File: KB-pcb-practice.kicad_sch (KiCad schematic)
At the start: 49 parts, among them J1 SWD, SW1 Boot, SW2 Reset, U1 NCP1117-3.3_SOT223, U1 W25Q128JVS, Y1 ABLS-12.000MHZ-B4-T

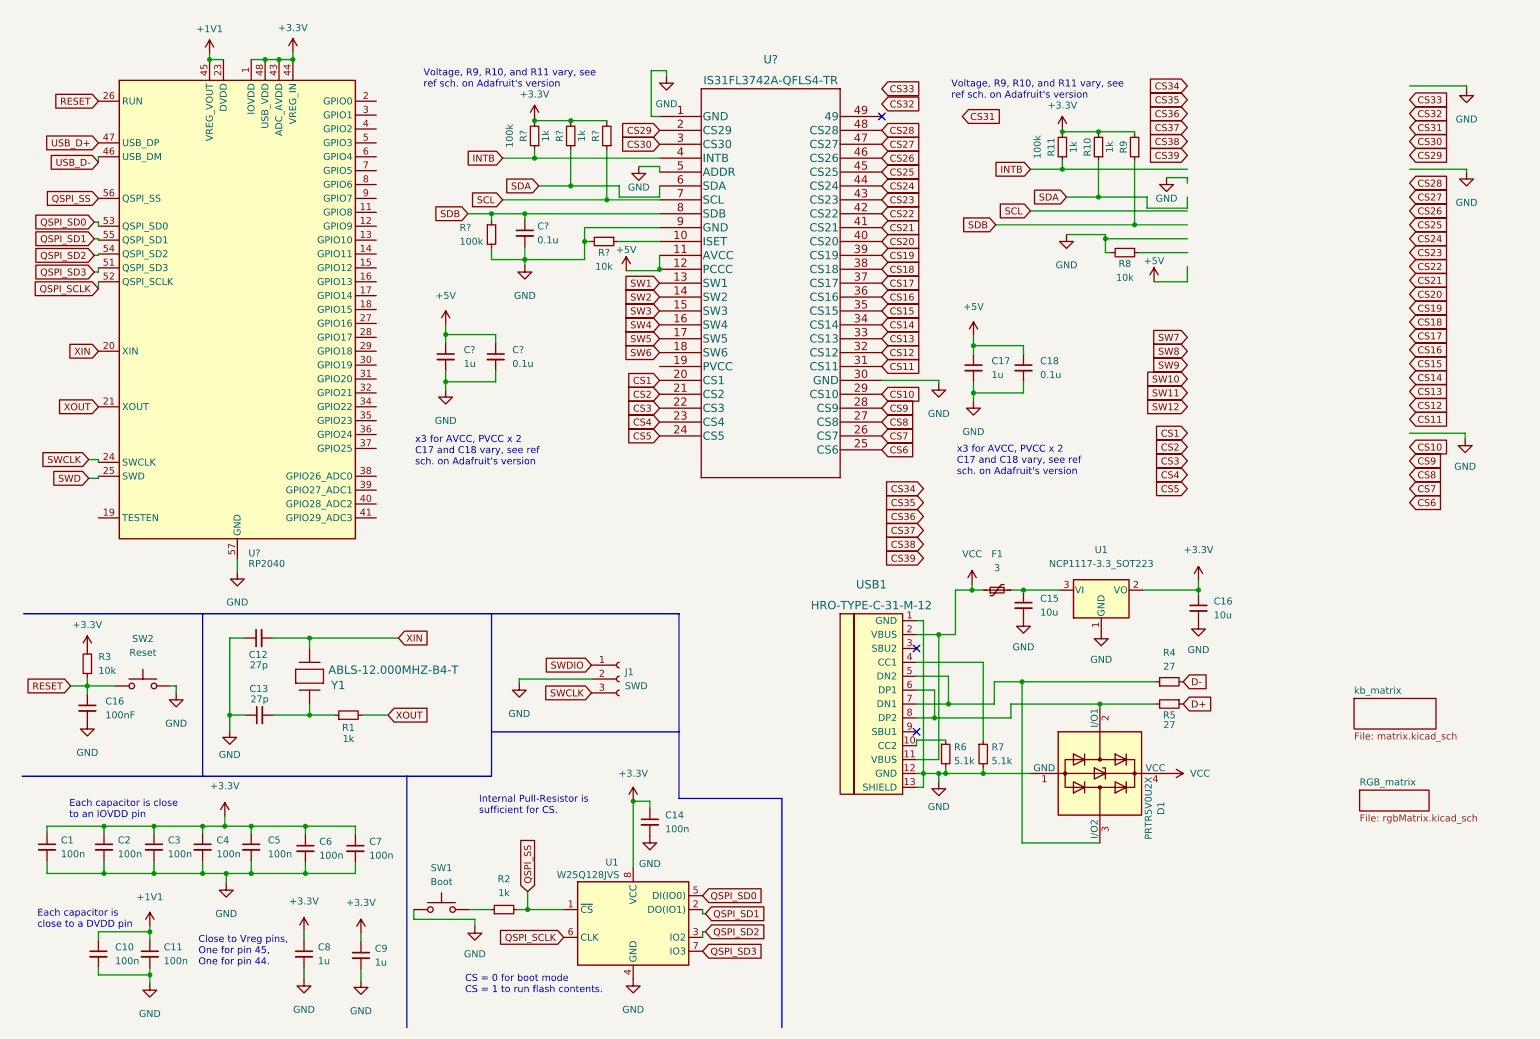
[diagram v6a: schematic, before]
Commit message: Finished Electric Schematic Of Keyboard
All components are now wired. Positions for spacers, button stabilizers, and threated holes not accounted.
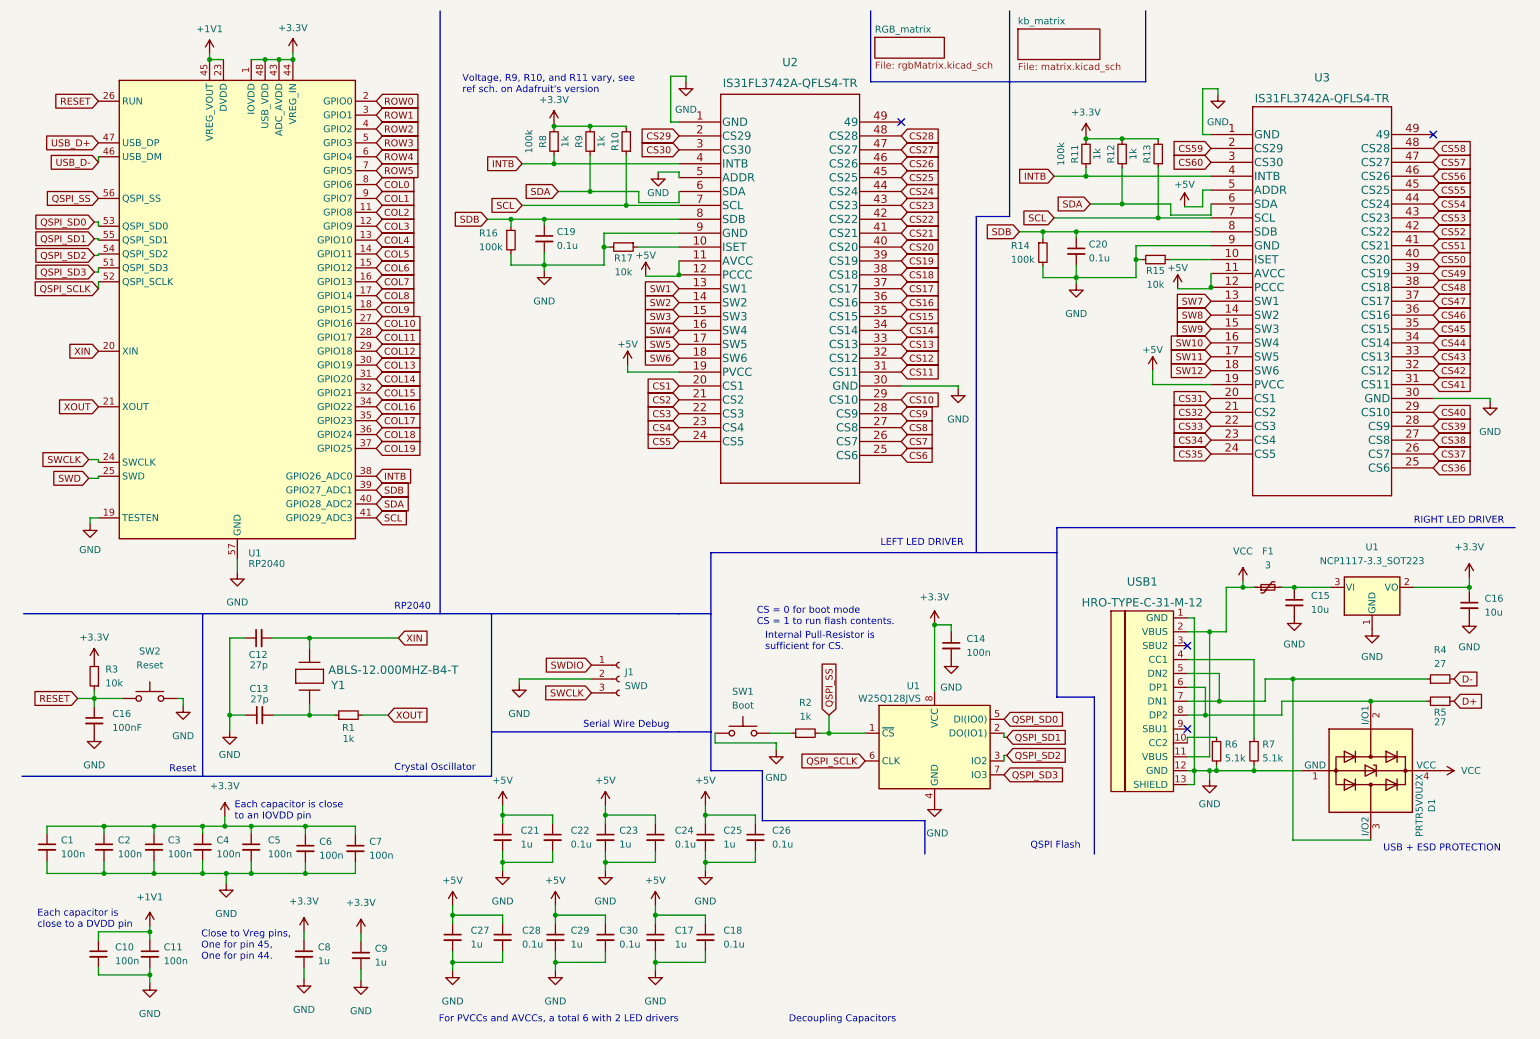
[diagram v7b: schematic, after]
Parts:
- removed R10, R9: 1k, symbol Device:R_Small
- removed R8: 10k, symbol Device:R_Small
- added C20, C22, C24, C26, C28: 0.1u, symbol Device:C_Small
- added C21, C23, C25, C27: 1u, symbol Device:C_Small
- added R12, R13: 1k, symbol Device:R_Small
- added R14: 100k, symbol Device:R_Small
- added R15: 10k, symbol Device:R_Small
- added U3: IS31FL3742A-QFLS4-TR, QFN48_IS31FL3742A-QFLS4-TR_ISI, symbol ul_IS31FL3742A-QFLS4-TR:IS31FL3742A-QFLS4-TR
- gave numbers to parts that had none: 10
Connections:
- net +3.3V: now also R12.2, R13.2
- net +5V: now also U2.19 (PVCC), C21.1, C22.1, C23.1, C24.1, C25.1, C26.1, C27.1, C28.1, U3.11 (AVCC), U3.12 (PCCC), U3.19 (PVCC), U3.5 (ADDR)
- net CS31: now also U3.20 (CS1)
- net CS32: now also U3.21 (CS2)
- net CS33: now also U3.22 (CS3)
- net CS34: now also U3.23 (CS4)
- net CS35: now also U3.24 (CS5)
- net CS36: now also U3.25 (CS6)
- net CS37: now also U3.26 (CS7)
- net CS38: now also U3.27 (CS8)
- net CS39: now also U3.28 (CS9)
- net GND: now also U1.19 (TESTEN), C20.2, C21.2, C22.2, C23.2, C24.2, C25.2, C26.2, C27.2, C28.2, R14.2, R15.2, U3.1 (GND), U3.30 (GND), U3.9 (GND)
- net INTB: now also U1.38 (GPIO26_ADC0), U3.4 (INTB)
- net SCL: now also U1.41 (GPIO29_ADC3), R13.1, U3.7 (SCL)
- net SDA: now also U1.40 (GPIO28_ADC2), R12.1, U3.6 (SDA)
- net SDB: now also U1.39 (GPIO27_ADC1), C20.1, R14.1, U3.8 (SDB)
- net SW10: now also U3.16 (SW4)
- net SW11: now also U3.17 (SW5)
- net SW12: now also U3.18 (SW6)
- net SW7: now also U3.13 (SW1)
- net SW8: now also U3.14 (SW2)
- net SW9: now also U3.15 (SW3)
- net COL2: now reaches U1.11 (GPIO8)
- net COL3: now reaches U1.12 (GPIO9)
- net COL4: now reaches U1.13 (GPIO10)
- net COL5: now reaches U1.14 (GPIO11)
- net COL6: now reaches U1.15 (GPIO12)
- net COL7: now reaches U1.16 (GPIO13)
- net COL8: now reaches U1.17 (GPIO14)
- net COL9: now reaches U1.18 (GPIO15)
- net ROW0: now reaches U1.2 (GPIO0)
- net COL10: now reaches U1.27 (GPIO16)
- net COL11: now reaches U1.28 (GPIO17)
- net COL12: now reaches U1.29 (GPIO18)
- net ROW1: now reaches U1.3 (GPIO1)
- net COL13: now reaches U1.30 (GPIO19)
- net COL14: now reaches U1.31 (GPIO20)
- net COL15: now reaches U1.32 (GPIO21)
- net COL16: now reaches U1.34 (GPIO22)
- net COL17: now reaches U1.35 (GPIO23)
- net COL18: now reaches U1.36 (GPIO24)
- net COL19: now reaches U1.37 (GPIO25)
- net ROW2: now reaches U1.4 (GPIO2)
- net ROW3: now reaches U1.5 (GPIO3)
- net ROW4: now reaches U1.6 (GPIO4)
- net ROW5: now reaches U1.7 (GPIO5)
- net COL0: now reaches U1.8 (GPIO6)
- net COL1: now reaches U1.9 (GPIO7)
- new net: R15.1, U3.10 (ISET)
- new net CS40: U3.29 (CS10)
- new net CS41: U3.31 (CS11)
- new net CS42: U3.32 (CS12)
- new net CS43: U3.33 (CS13)
- new net CS44: U3.34 (CS14)
- new net CS45: U3.35 (CS15)
- new net CS46: U3.36 (CS16)
- new net CS47: U3.37 (CS17)
- new net CS48: U3.38 (CS18)
- new net CS49: U3.39 (CS19)
- new net CS50: U3.40 (CS20)
- new net CS51: U3.41 (CS21)
- new net CS52: U3.42 (CS22)
- new net CS53: U3.43 (CS23)
- new net CS54: U3.44 (CS24)
- new net CS55: U3.45 (CS25)
- new net CS56: U3.46 (CS26)
- new net CS57: U3.47 (CS27)
- new net CS58: U3.48 (CS28)
- new net CS59: U3.2 (CS29)
- new net CS60: U3.3 (CS30)
- no-connect marks 3 -> 4
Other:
- note added: "Crystal Oscillator"
- note added: "Decoupling Capacitors"
- note added: "For PVCCs and AVCCs, a total 6 with 2 LED drivers"
- note added: "LEFT LED DRIVER"
- note added: "QSPI Flash"
- note added: "RIGHT LED DRIVER"
- note added: "RP2040"
- note added: "Reset"
- note added: "Serial Wire Debug"
- note added: "USB + ESD PROTECTION"
- note removed: "x3 for AVCC, PVCC x 2 C17 and C18 vary, see ref sch. on Adafruit's version"
- moved on the sheet: C14, C15, C16, C19, C29, C30, D1, F1, R10, R16, R17, R2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

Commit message: Started work on PCB layout
Slightly Adjusted electric schematic as well.
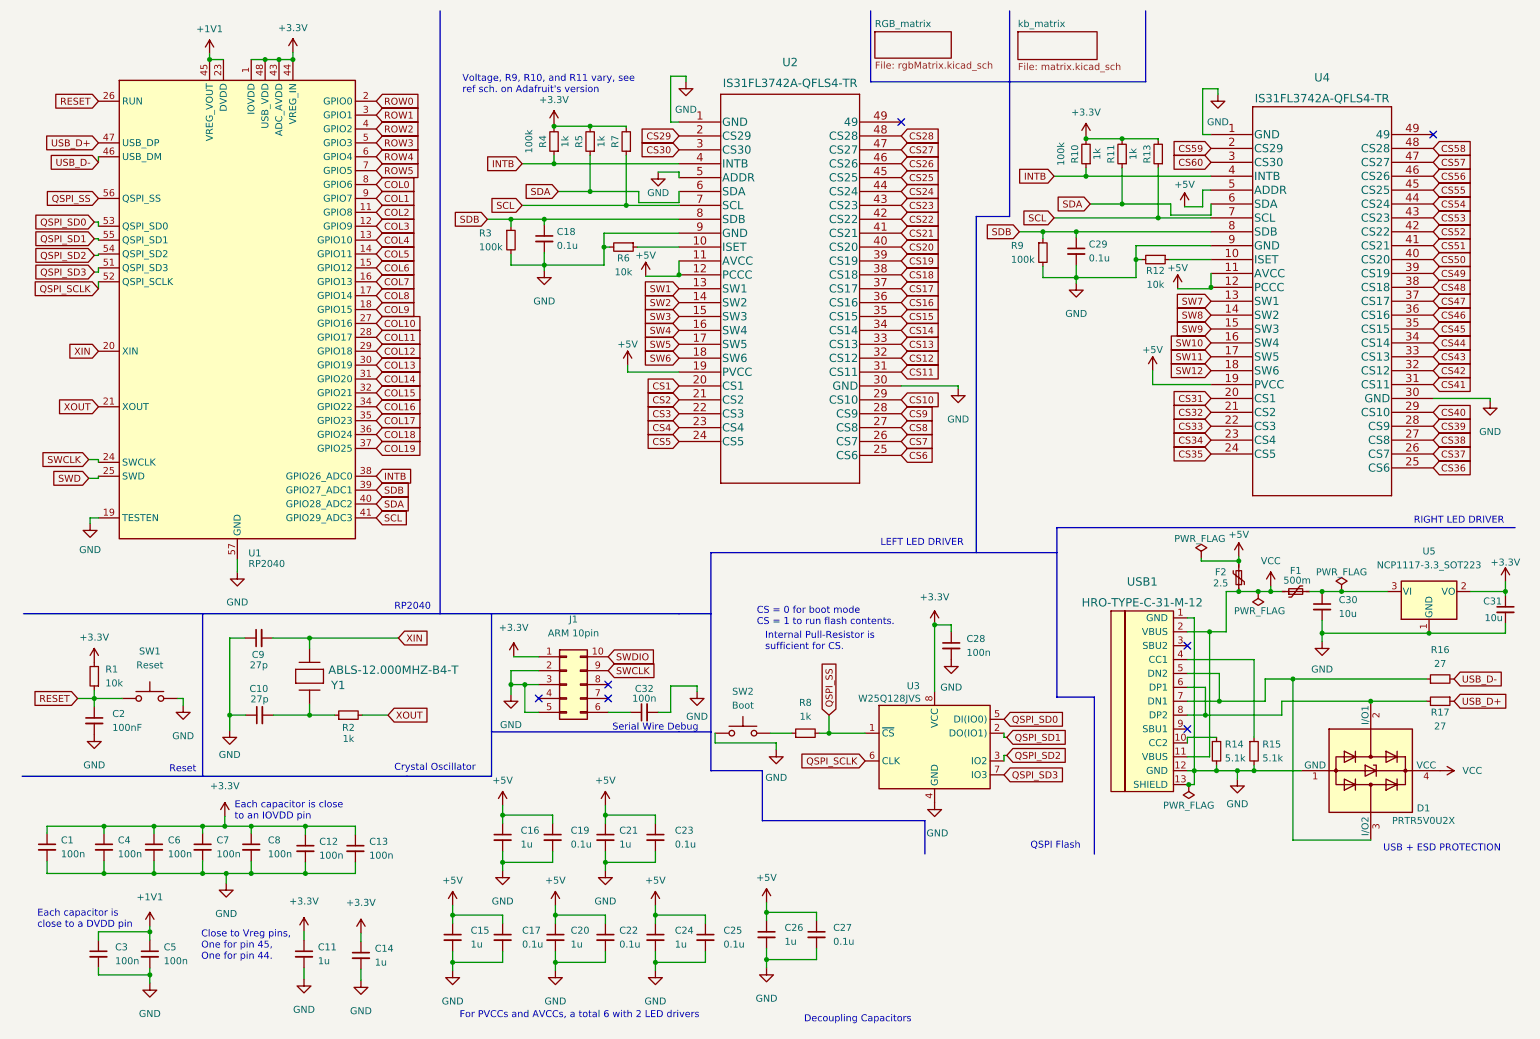
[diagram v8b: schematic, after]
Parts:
- removed J1: SWD, symbol Connector:Conn_01x03_Female
- added C32: 100n, Capacitor_SMD:C_0805_2012Metric_Pad1.18x1.45mm_HandSolder, symbol Device:C_Small
- added F2: 2.5, Fuse:Fuse_1206_3216Metric_Pad1.42x1.75mm_HandSolder, symbol Device:Polyfuse_Small
- added J1: ARM 10pin, Connector_PinHeader_1.27mm:PinHeader_2x05_P1.27mm_Horizontal, symbol Connector_Generic:Conn_02x05_Counter_Clockwise
- C1: footprint (none) -> Capacitor_SMD:C_0805_2012Metric_Pad1.18x1.45mm_HandSolder
- C10: renamed from C13; footprint (none) -> Capacitor_SMD:C_0805_2012Metric_Pad1.18x1.45mm_HandSolder
- C11: renamed from C8; footprint (none) -> Capacitor_SMD:C_0805_2012Metric_Pad1.18x1.45mm_HandSolder
- C12: renamed from C6; footprint (none) -> Capacitor_SMD:C_0805_2012Metric_Pad1.18x1.45mm_HandSolder
- C13: renamed from C7; footprint (none) -> Capacitor_SMD:C_0805_2012Metric_Pad1.18x1.45mm_HandSolder
- C14: renamed from C9; footprint (none) -> Capacitor_SMD:C_0805_2012Metric_Pad1.18x1.45mm_HandSolder
- C15: renamed from C27; footprint (none) -> Capacitor_SMD:C_0805_2012Metric_Pad1.18x1.45mm_HandSolder
- C16: renamed from C21; footprint (none) -> Capacitor_SMD:C_0805_2012Metric_Pad1.18x1.45mm_HandSolder
- C17: renamed from C28; footprint (none) -> Capacitor_SMD:C_0805_2012Metric_Pad1.18x1.45mm_HandSolder
- C18: renamed from C19; footprint (none) -> Capacitor_SMD:C_0805_2012Metric_Pad1.18x1.45mm_HandSolder
- C19: renamed from C22; footprint (none) -> Capacitor_SMD:C_0805_2012Metric_Pad1.18x1.45mm_HandSolder
- C2, C31: renamed from C16; footprint (none) -> Capacitor_SMD:C_0805_2012Metric_Pad1.18x1.45mm_HandSolder
- C20: renamed from C29; footprint (none) -> Capacitor_SMD:C_0805_2012Metric_Pad1.18x1.45mm_HandSolder
- C21: renamed from C23; footprint (none) -> Capacitor_SMD:C_0805_2012Metric_Pad1.18x1.45mm_HandSolder
- C22: renamed from C30; footprint (none) -> Capacitor_SMD:C_0805_2012Metric_Pad1.18x1.45mm_HandSolder
- C23: renamed from C24; footprint (none) -> Capacitor_SMD:C_0805_2012Metric_Pad1.18x1.45mm_HandSolder
- C24: renamed from C17; footprint (none) -> Capacitor_SMD:C_0805_2012Metric_Pad1.18x1.45mm_HandSolder
- C25: renamed from C18; footprint (none) -> Capacitor_SMD:C_0805_2012Metric_Pad1.18x1.45mm_HandSolder
- C26: renamed from C25; footprint (none) -> Capacitor_SMD:C_0805_2012Metric_Pad1.18x1.45mm_HandSolder
- C27: renamed from C26; footprint (none) -> Capacitor_SMD:C_0805_2012Metric_Pad1.18x1.45mm_HandSolder
- C28: renamed from C14; footprint (none) -> Capacitor_SMD:C_0805_2012Metric_Pad1.18x1.45mm_HandSolder
- C29: renamed from C20; footprint (none) -> Capacitor_SMD:C_0805_2012Metric_Pad1.18x1.45mm_HandSolder
- C3: renamed from C10; footprint (none) -> Capacitor_SMD:C_0805_2012Metric_Pad1.18x1.45mm_HandSolder
- C30: renamed from C15; footprint (none) -> Capacitor_SMD:C_0805_2012Metric_Pad1.18x1.45mm_HandSolder
- C4: renamed from C2; footprint (none) -> Capacitor_SMD:C_0805_2012Metric_Pad1.18x1.45mm_HandSolder
- C5: renamed from C11; footprint (none) -> Capacitor_SMD:C_0805_2012Metric_Pad1.18x1.45mm_HandSolder
- C6: renamed from C3; footprint (none) -> Capacitor_SMD:C_0805_2012Metric_Pad1.18x1.45mm_HandSolder
- C7: renamed from C4; footprint (none) -> Capacitor_SMD:C_0805_2012Metric_Pad1.18x1.45mm_HandSolder
- C8: renamed from C5; footprint (none) -> Capacitor_SMD:C_0805_2012Metric_Pad1.18x1.45mm_HandSolder
- C9: renamed from C12; footprint (none) -> Capacitor_SMD:C_0805_2012Metric_Pad1.18x1.45mm_HandSolder
- F1: value 3 -> 500m; footprint (none) -> Fuse:Fuse_1206_3216Metric_Pad1.42x1.75mm_HandSolder
- R1: renamed from R3; footprint (none) -> Resistor_SMD:R_0805_2012Metric_Pad1.20x1.40mm_HandSolder
- R10: renamed from R11; footprint (none) -> Resistor_SMD:R_0805_2012Metric_Pad1.20x1.40mm_HandSolder
- R11: renamed from R12; footprint (none) -> Resistor_SMD:R_0805_2012Metric_Pad1.20x1.40mm_HandSolder
- R12: renamed from R15; footprint (none) -> Resistor_SMD:R_0805_2012Metric_Pad1.20x1.40mm_HandSolder
- R13: footprint (none) -> Resistor_SMD:R_0805_2012Metric_Pad1.20x1.40mm_HandSolder
- R14: renamed from R6; footprint (none) -> Resistor_SMD:R_0805_2012Metric_Pad1.20x1.40mm_HandSolder
- R15: renamed from R7; footprint (none) -> Resistor_SMD:R_0805_2012Metric_Pad1.20x1.40mm_HandSolder
- R16: renamed from R4; footprint (none) -> Resistor_SMD:R_0805_2012Metric_Pad1.20x1.40mm_HandSolder
- R17: renamed from R5; footprint (none) -> Resistor_SMD:R_0805_2012Metric_Pad1.20x1.40mm_HandSolder
- R2: renamed from R1; footprint (none) -> Resistor_SMD:R_0805_2012Metric_Pad1.20x1.40mm_HandSolder
- R3: renamed from R16; footprint (none) -> Resistor_SMD:R_0805_2012Metric_Pad1.20x1.40mm_HandSolder
- R4: renamed from R8; footprint (none) -> Resistor_SMD:R_0805_2012Metric_Pad1.20x1.40mm_HandSolder
- R5: renamed from R9; footprint (none) -> Resistor_SMD:R_0805_2012Metric_Pad1.20x1.40mm_HandSolder
- R6: renamed from R17; footprint (none) -> Resistor_SMD:R_0805_2012Metric_Pad1.20x1.40mm_HandSolder
- R7: renamed from R10; footprint (none) -> Resistor_SMD:R_0805_2012Metric_Pad1.20x1.40mm_HandSolder
- R8: renamed from R2; footprint (none) -> Resistor_SMD:R_0805_2012Metric_Pad1.20x1.40mm_HandSolder
- R9: renamed from R14; footprint (none) -> Resistor_SMD:R_0805_2012Metric_Pad1.20x1.40mm_HandSolder
- SW1: renamed from SW2; footprint (none) -> Button_Switch_SMD:SW_SPST_SKQG_WithStem
- SW2: renamed from SW1; footprint (none) -> Button_Switch_SMD:SW_SPST_SKQG_WithStem
- U2: footprint QFN48_IS31FL3742A-QFLS4-TR_ISI -> ul_IS31FL3742A-QFLS4-TR:IS31FL3742A-QFLS4-TR
- U4: renamed from U3; footprint QFN48_IS31FL3742A-QFLS4-TR_ISI -> ul_IS31FL3742A-QFLS4-TR:IS31FL3742A-QFLS4-TR
- USB1: footprint (none) -> Type-C:HRO-TYPE-C-31-M-12-HandSoldering
- Y1: footprint XTAL_ABLS_ABR -> ABLS-12-MHZ-B4-T:ABLS-12.000MHZ-B4-T
- renumbered U1 to U3, U1 to U5
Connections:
- net D+ is gone; now on net USB_D+: R17.1
- net D- is gone; now on net USB_D-: R16.2
- net +3.3V: now also J1.1 (Pin_1)
- net +5V: now also F2.2
- net GND: now also C32.2, J1.2 (Pin_2), J1.3 (Pin_3), J1.5 (Pin_5)
- net SWCLK: now also J1.9 (Pin_9)
- net SWDIO: now also J1.10 (Pin_10)
- net VCC: now also F2.1
- new net: C32.1, J1.6 (Pin_6)
- no-connect marks 4 -> 7
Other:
- moved on the sheet: C26, C27, C30, C31, F1, U5
